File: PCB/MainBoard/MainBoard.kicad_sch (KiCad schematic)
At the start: 13 parts, among them Q1 PT334-6C, SW1 SW_DIP_x05, U1 LM393, U2 ESP32-WROOM-32

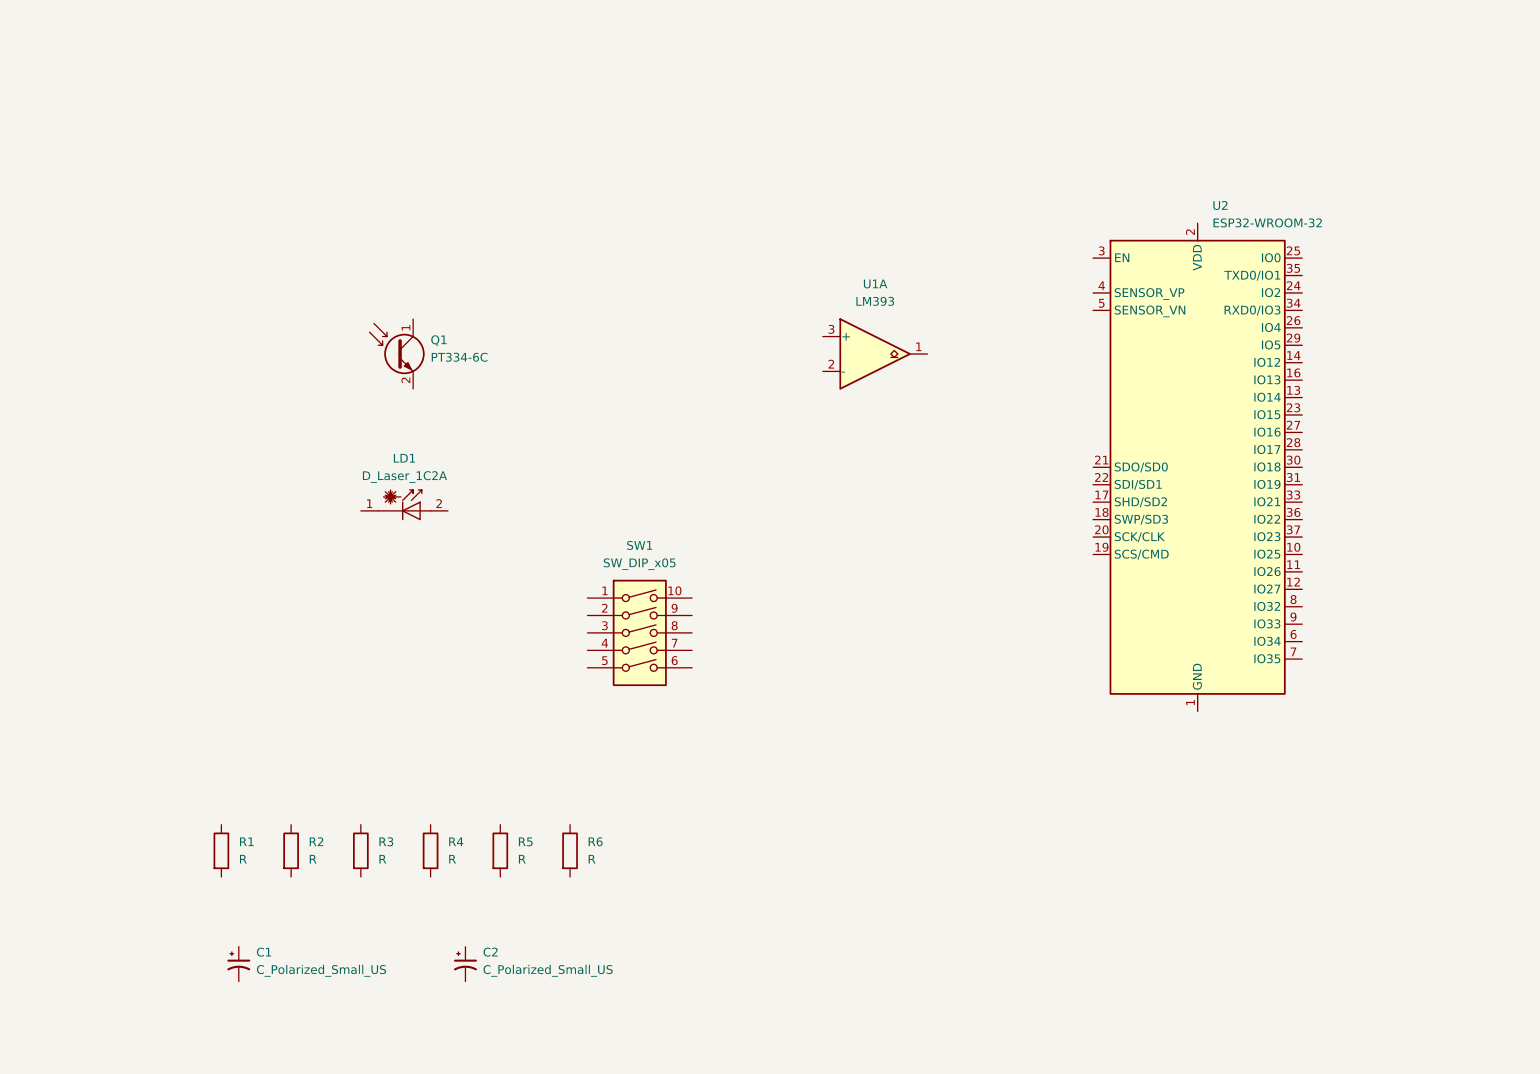
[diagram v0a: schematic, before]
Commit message: Refactor README and add user journey documentation for curling timer system
- Updated GATT service model section in README to emphasize structured data exchange and real-time updates.
- Created a semi-comprehensive user journey document detailing preconfiguration, setup, operation, and maintenance processes for the curling timer system.
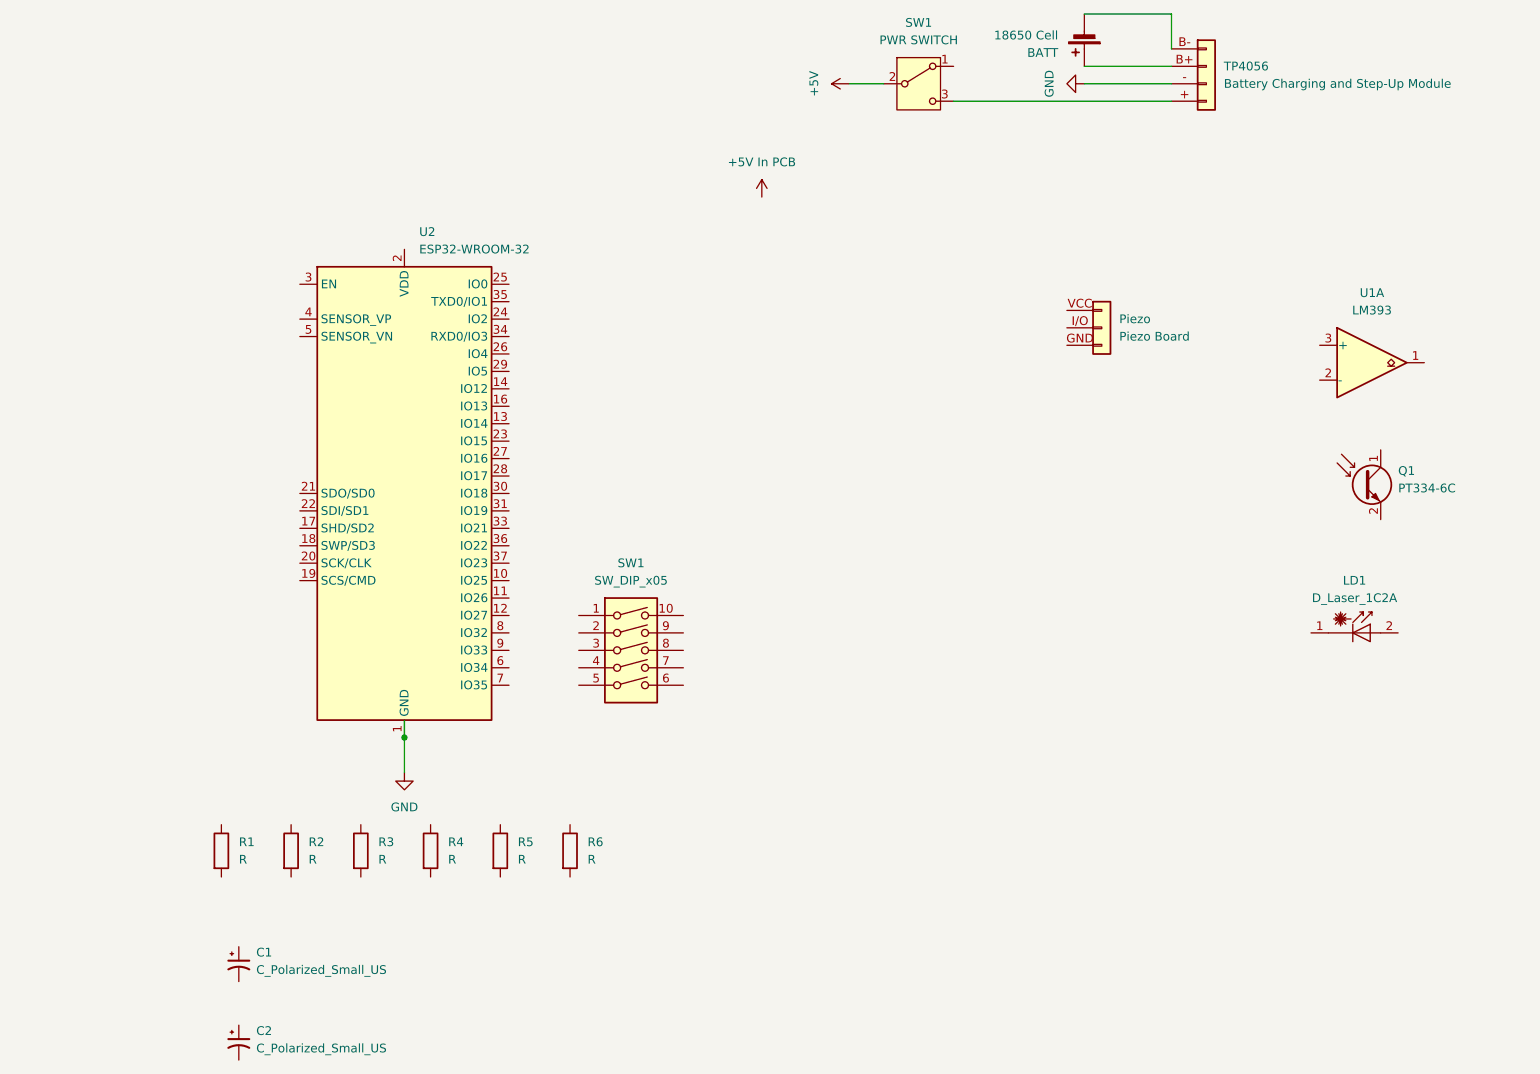
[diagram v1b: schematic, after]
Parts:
- added BATT: 18650 Cell, symbol Device:Battery_Cell
- added Piezo: Piezo Board, symbol Connector_Generic:Conn_01x03
- added SW1: PWR SWITCH, symbol Switch:SW_SPDT
- added TP4056: Battery Charging and Step-Up Module, symbol Connector_Generic:Conn_01x04
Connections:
- net GND: now reaches U2.1 (GND), U2.15 (GND), U2.38 (GND), U2.39 (GND)
- net GND: now also TP4056.- (Out-)
- new net: SW1.3 (C), TP4056.+ (Out+)
- new net: BATT.1 (+), TP4056.B+ (Batt+)
- new net: BATT.2 (-), TP4056.B- (Batt-)
- new net +5V: SW1.2 (B)
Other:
- moved on the sheet: C2, LD1, Q1, SW1, U1A, U2

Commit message: Iniital schematic (poor layout), and added additional functionality to the firmware
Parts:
- removed Piezo: Piezo Board, symbol Connector_Generic:Conn_01x03
- added LS1: Active Piezo, CMI-1295IC-0585T:CUI_CMI-1295IC-0585T, symbol CMI-1295IC-0585T Piezo:CMI-1295IC-0585T
- added Q2: NPN, symbol Simulation_SPICE:NPN
- added R7: 100kΩ, symbol Device:R
- added R8: 47kΩ, symbol Device:R
- added unit 3 of U1
- C1, C2: value C_Polarized_Small_US -> 0.1µF
- R1, R2: value R -> 100kΩ
- R3, R5: value R -> 10kΩ
- R4: value R -> 1MΩ
- R6: value R -> 1kΩ
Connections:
- net +5V In PCB: now also LD1.2 (A), U2.2 (VDD), LS1.
- net GND: now also C1.2, C2.2, LD1.1 (K), Q1.2 (E), R1.2, Q2.3 (E), R8.2, U1.4 (V-)
- net +3V3: now reaches C1.1
- net +3V3: now also R2.2, R3.2, R5.2, SW1.10, SW1.6, SW1.7, SW1.8, SW1.9, U1.8 (V+)
- net at R1.1: now also R2.1, U1.2 (-)
- net at R5.1: now also R4.1, U1.1, U2.33 (IO21)
- net at Q1.1 (C): now also C2.1, R3.1, R4.2, U1.3 (+)
- net at U2.10 (IO25): now also SW1.3
- net at U2.11 (IO26): now also SW1.4
- net at U2.12 (IO27): now also SW1.5
- net at U2.31 (IO19): now also R6.2
- net at U2.36 (IO22): now also SW1.1
- net at U2.37 (IO23): now also SW1.2
- net at U2.7 (IO35): now also R7.2, R8.1
- net at R6.1: now also Q2.2 (B)
- net at BATT.1 (+), TP4056.B+ (Batt+): now also R7.1
- new net: LS1., Q2.1 (C)
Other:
- moved on the sheet: BATT, C1, C2, LD1, Q1, R1, R2, R3, R4, R5, R6, SW1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

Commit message: Lots of changes - initial pcb layout without wires
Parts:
- C1, C2: footprint (none) -> Capacitor_THT:C_Disc_D5.0mm_W2.5mm_P5.00mm
- LD1: footprint (none) -> LED_THT:LED_D5.0mm_Horizontal_O1.27mm_Z3.0mm_Clear
- LS1: footprint CMI-1295IC-0585T:CUI_CMI-1295IC-0585T -> FSCT:CUI_CMI-1295IC-0585T
- Q2: footprint (none) -> FSCT:TO92127P476H533-3
- R1, R2, R3, R4, R5, R6, R7, R8: footprint (none) -> Resistor_THT:R_Axial_DIN0204_L3.6mm_D1.6mm_P7.62mm_Horizontal
- SW2: renamed from SW1; footprint (none) -> Button_Switch_THT:SW_DIP_SPSTx05_Slide_9.78x14.88mm_W7.62mm_P2.54mm
- U1: footprint (none) -> LM393N:DIP254P762X508-8
- renumbered BATT to BATT1
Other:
- moved on the sheet: Q1
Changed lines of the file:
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@@
 	)
 	(junction
-		(at 196.85 73.66)
-		(diameter 0)
-		(color 0 0 0 0)
-	)
-	(junction
 		(at 50.8 123.19)
 		(diameter 0)
@@
 	)
 	(junction
+		(at 196.85 73.66)
+		(diameter 0)
+		(color 0 0 0 0)
+	)
+	(junction
 		(at 191.77 101.6)
 		(diameter 0)
@@
 	(wire
 		(pts
+			(xy 196.85 46.99) (xy 77.47 46.99)
+		)
+		(stroke
+			(width 0)
+			(type default)
+		)
+	)
+	(wire
+		(pts
 			(xy 160.02 68.58) (xy 160.02 73.66)
 		)
@@
 	(wire
 		(pts
-			(xy 182.88 69.85) (xy 186.69 69.85)
+			(xy 63.5 46.99) (xy 67.31 46.99)
 		)
 		(stroke
@@
 	(wire
 		(pts
-			(xy 196.85 69.85) (xy 196.85 73.66)
+			(xy 196.85 46.99) (xy 196.85 73.66)
 		)
 		(stroke
@@
 	(symbol
 		(lib_id "power:GND")
-		(at 182.88 69.85 270)
+		(at 63.5 46.99 270)
 		(unit 1)
 		(exclude_from_sim no)
@@
 		(dnp no)
 		(property "Reference" "#PWR07"
-			(at 176.53 69.85 0)
+			(at 57.15 46.99 0)
 			(effects
 				(font
@@
 		)
 		(property "Value" "GND"
-			(at 177.8 69.85 0)
+			(at 58.42 46.99 0)
 			(effects
 				(font
@@
 		)
 		(property "Footprint" ""
-			(at 182.88 69.85 0)
+			(at 63.5 46.99 0)
 			(effects
 				(font
@@
 		)
 		(property "Datasheet" ""
-			(at 182.88 69.85 0)
+			(at 63.5 46.99 0)
 			(effects
 				(font
@@
 		)
 		(property "Description" "Power symbol creates a global label with name \"GND\" , ground"
-			(at 182.88 69.85 0)
+			(at 63.5 46.99 0)
 			(effects
 				(font
@@
 			)
 		)
-		(property "Footprint" ""
+		(property "Footprint" "Capacitor_THT:C_Disc_D5.0mm_W2.5mm_P5.00mm"
 			(at 181.61 85.09 0)
 			(effects
@@
 			)
 		)
-		(property "Footprint" ""
+		(property "Footprint" "LM393N:DIP254P762X508-8"
 			(at 181.61 78.74 0)
 			(effects
@@
 			)
 		)
-		(property "Footprint" ""
+		(property "Footprint" "Resistor_THT:R_Axial_DIN0204_L3.6mm_D1.6mm_P7.62mm_Horizontal"
 			(at 154.432 90.17 90)
 			(effects
@@
 		(exclude_from_sim no)
 		(in_bom yes)
-		(on_board yes)
+		(on_board no)
 		(dnp no)
 		(fields_autoplaced yes)
@@
 			)
 		)
-		(property "Footprint" ""
+		(property "Footprint" "Resistor_THT:R_Axial_DIN0204_L3.6mm_D1.6mm_P7.62mm_Horizontal"
 			(at 148.59 105.918 90)
 			(effects
@@
 	(symbol
 		(lib_id "Sensor_Optical:BPW40")
-		(at 191.77 67.31 270)
+		(at 72.39 44.45 270)
 		(unit 1)
 		(exclude_from_sim no)
@@
 		(fields_autoplaced yes)
 		(property "Reference" "Q1"
-			(at 192.5193 58.42 90)
+			(at 73.1393 35.56 90)
 			(effects
 				(font
@@
 		)
 		(property "Value" "PT334-6C"
-			(at 192.5193 60.96 90)
+			(at 73.1393 38.1 90)
 			(effects
 				(font
@@
 		)
 		(property "Footprint" "LED_THT:LED_D5.0mm_Horizontal_O1.27mm_Z3.0mm_Clear"
-			(at 188.214 79.502 0)
+			(at 68.834 56.642 0)
 			(effects
 				(font
@@
 		)
 		(property "Datasheet" "https://www.rcscomponents.kiev.ua/datasheets/bpw40.pdf"
-			(at 191.77 67.31 0)
+			(at 72.39 44.45 0)
 			(effects
 				(font
@@
 		)
 		(property "Description" "Phototransistor NPN"
-			(at 191.77 67.31 0)
+			(at 72.39 44.45 0)
 			(effects
 				(font
@@
 		(exclude_from_sim no)
 		(in_bom yes)
-		(on_board yes)
+		(on_board no)
 		(dnp no)
 		(property "Reference" "U2"
@@
 			)
 		)
-		(property "Footprint" ""
+		(property "Footprint" "LM393N:DIP254P762X508-8"
 			(at 151.13 76.2 0)
 			(effects
@@
 			)
 		)
-		(property "Footprint" ""
+		(property "Footprint" "Resistor_THT:R_Axial_DIN0204_L3.6mm_D1.6mm_P7.62mm_Horizontal"
 			(at 159.512 90.17 90)
 			(effects
@@
 		(on_board yes)
 		(dnp no)
-		(property "Reference" "SW1"
+		(property "Reference" "SW2"
 			(at 152.4 124.968 0)
 			(effects
@@
 			)
 		)
-		(property "Footprint" ""
+		(property "Footprint" "Button_Switch_THT:SW_DIP_SPSTx05_Slide_9.78x14.88mm_W7.62mm_P2.54mm"
 			(at 152.4 115.57 0)
 			(effects
@@
 			(project ""
 				(path "/274a095b-f165-429e-9527-e47407a5037a"
-					(reference "SW1")
+					(reference "SW2")
 					(unit 1)
 				)
@@
 			)
 		)
-		(property "Footprint" "CMI-1295IC-0585T:CUI_CMI-1295IC-0585T"
+		(property "Footprint" "FSCT:CUI_CMI-1295IC-0585T"
 			(at 142.24 57.15 0)
 			(effects
@@
 			)
 		)
-		(property "Footprint" ""
+		(property "Footprint" "Resistor_THT:R_Axial_DIN0204_L3.6mm_D1.6mm_P7.62mm_Horizontal"
 			(at 195.072 86.36 90)
 			(effects
@@
 			)
 		)
-		(property "Footprint" ""
+		(property "Footprint" "LED_THT:LED_D5.0mm_Horizontal_O1.27mm_Z3.0mm_Clear"
 			(at 71.12 60.325 0)
 			(effects
@@
 			)
 		)
-		(property "Footprint" ""
+		(property "Footprint" "Resistor_THT:R_Axial_DIN0204_L3.6mm_D1.6mm_P7.62mm_Horizontal"
 			(at 151.13 70.358 90)
 			(effects
@@
 			)
 		)
-		(property "Footprint" ""
+		(property "Footprint" "Resistor_THT:R_Axial_DIN0204_L3.6mm_D1.6mm_P7.62mm_Horizontal"
 			(at 90.17 142.748 90)
 			(effects
@@
 			)
 		)
-		(property "Footprint" ""
+		(property "Footprint" "Resistor_THT:R_Axial_DIN0204_L3.6mm_D1.6mm_P7.62mm_Horizontal"
 			(at 132.842 90.17 90)
 			(effects
@@
 			)
 		)
-		(property "Footprint" ""
+		(property "Footprint" "FSCT:TO92127P476H533-3"
 			(at 134.62 12.7 0)
 			(effects
@@
 			)
 		)
-		(property "Footprint" ""
+		(property "Footprint" "Resistor_THT:R_Axial_DIN0204_L3.6mm_D1.6mm_P7.62mm_Horizontal"
 			(at 77.47 142.748 90)
 			(effects
@@
 		(exclude_from_sim no)
 		(in_bom yes)
-		(on_board yes)
+		(on_board no)
 		(dnp no)
 		(property "Reference" "TP4056"
@@
 			)
 		)
-		(property "Footprint" ""
+		(property "Footprint" "Capacitor_THT:C_Disc_D5.0mm_W2.5mm_P5.00mm"
 			(at 166.37 77.47 0)
 			(effects
@@
 		(exclude_from_sim no)
 		(in_bom yes)
-		(on_board yes)
+		(on_board no)
 		(dnp no)
 		(fields_autoplaced yes)
-		(property "Reference" "BATT"
+		(property "Reference" "BATT1"
 			(at 52.7684 114.3 0)
 			(effects
@@
 			(project ""
 				(path "/274a095b-f165-429e-9527-e47407a5037a"
-					(reference "BATT")
+					(reference "BATT1")
 					(unit 1)
 				)

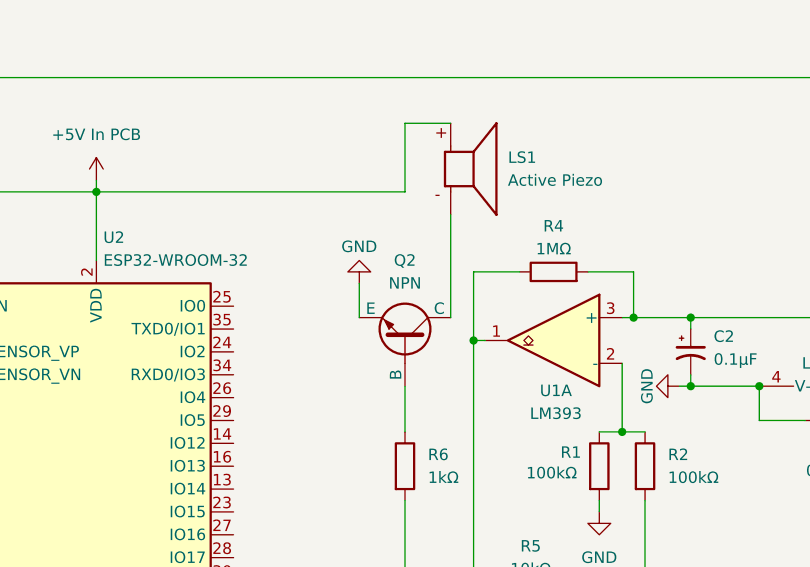
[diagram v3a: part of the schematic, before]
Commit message: PCB v1.0 - schematic needs review still in comparison to PCB - initial order of PCBs with JLCPCB. Updated BOM to reflect actual resistor/capacitor count.
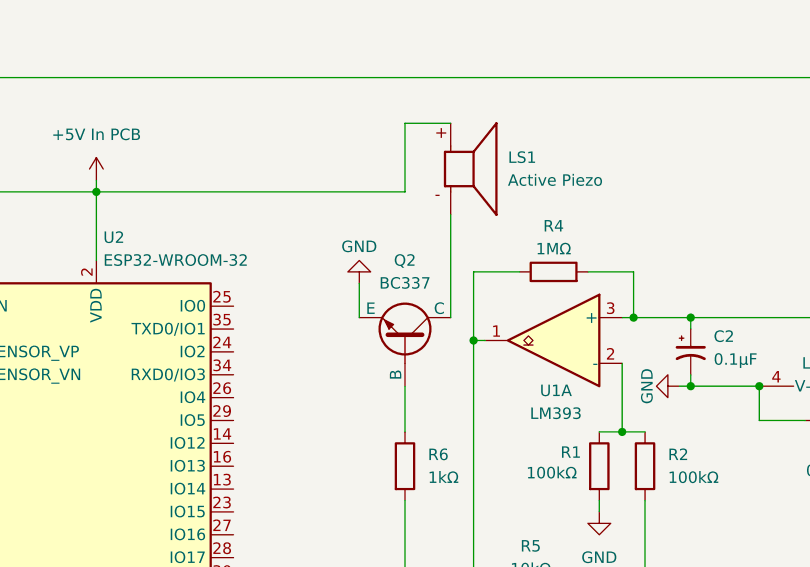
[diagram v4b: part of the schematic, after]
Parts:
- Q2: value NPN -> BC337
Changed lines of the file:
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@@
 			)
 		)
-		(property "Value" "NPN"
+		(property "Value" "BC337"
 			(at 134.62 69.85 90)
 			(effects
